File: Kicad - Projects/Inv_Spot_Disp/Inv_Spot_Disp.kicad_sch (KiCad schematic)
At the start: 44 parts, among them J1 PWM_Out, J2 Power_Supply, J3 Current_Sense, J4 Prog, SW1 1, SW2 2, SW3 3, SW4 4, SW5 SW_Push, U1 STM32F030F4Px, U2 NHD-0420H1Z, U3 AMS1117-3.3, U4 LKS561, U5 LM358, U6 LTV-817S

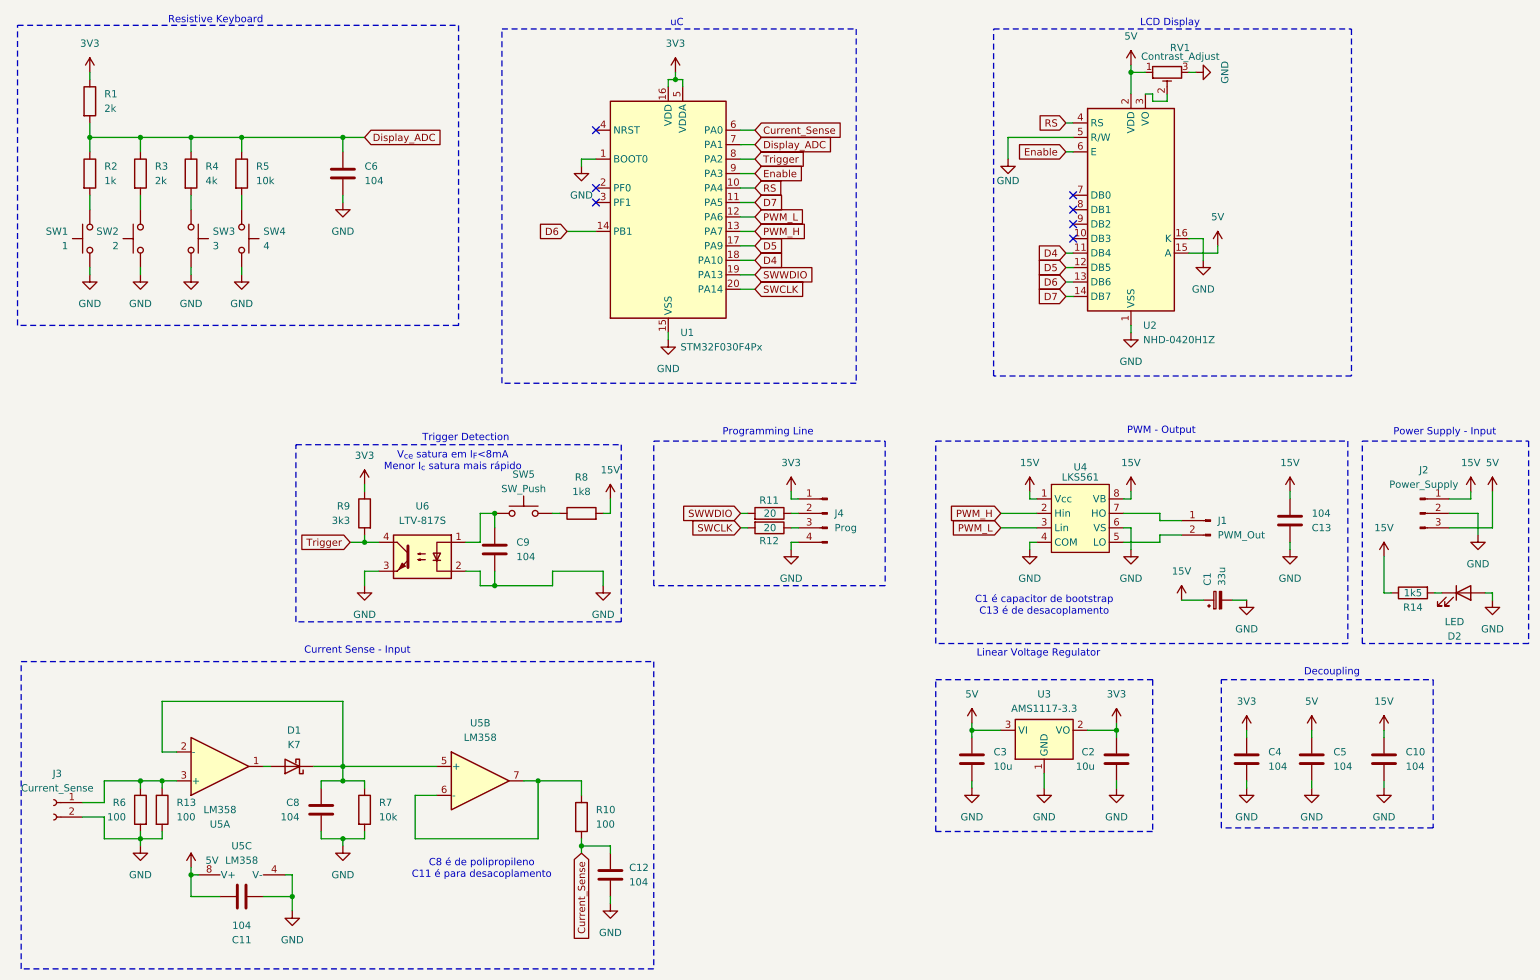
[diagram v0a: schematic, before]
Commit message: Semi-final Touches
Menu now uses power instead of current

Removed pulsed timing from "CARVAO" and "ARRUELA" operation modes

Added parafix mode

Fixed schematic for output transformer

Added rectification on the output

Trying different power trace geometry in antecipation of voltage spikes
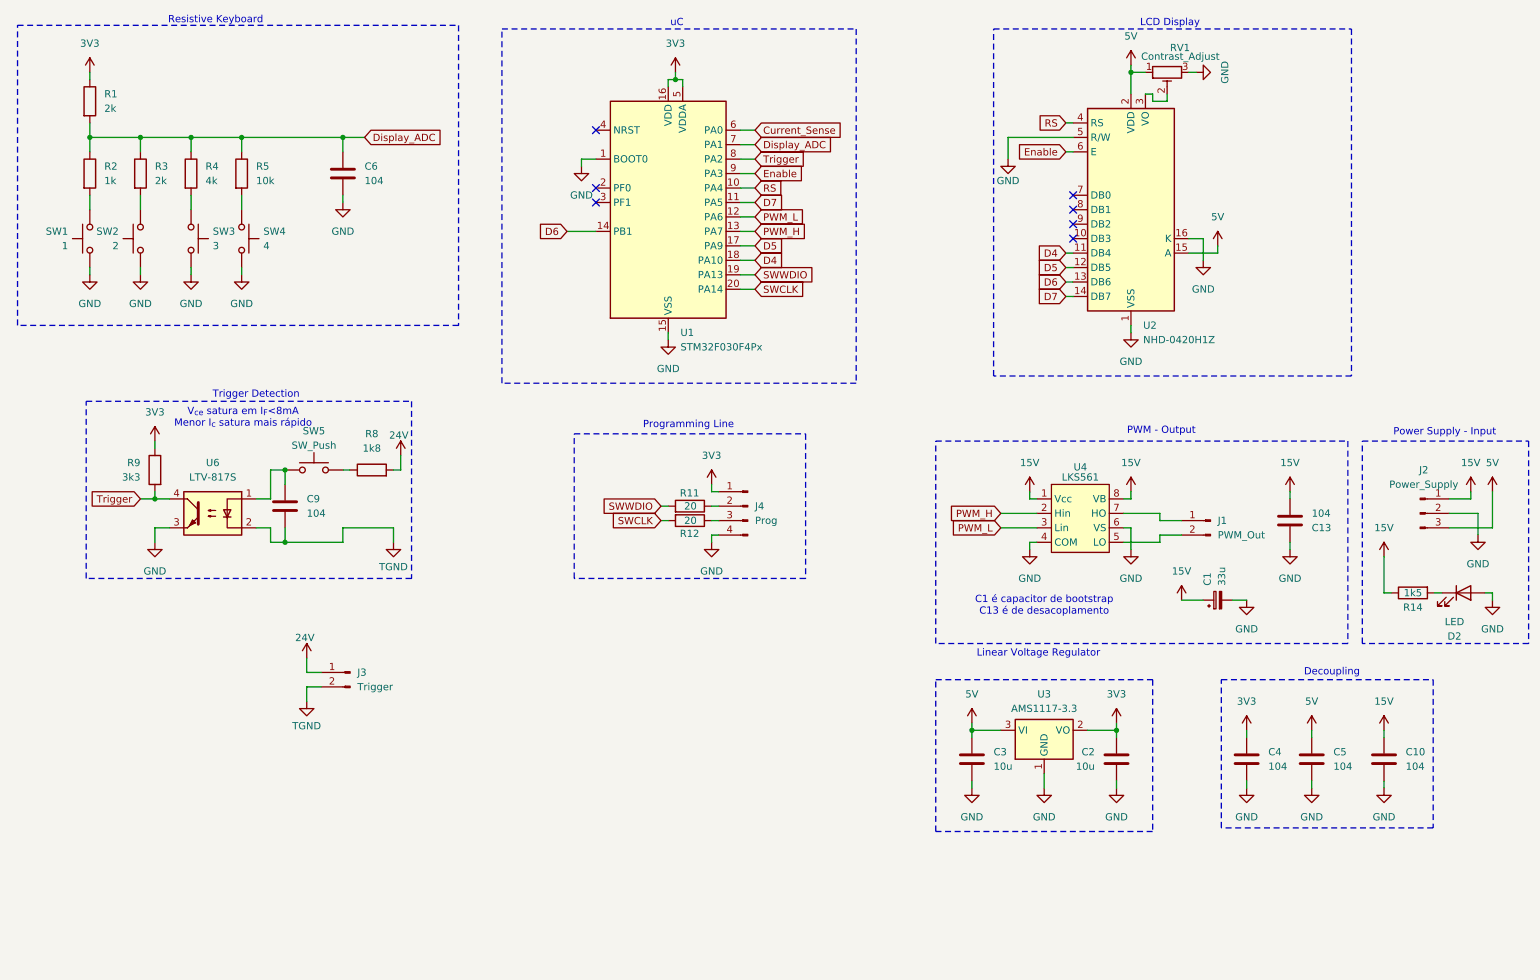
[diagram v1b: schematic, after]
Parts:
- removed C11, C12: 104, Capacitor_SMD:C_1206_3216Metric_Pad1.33x1.80mm_HandSolder, symbol Device:C
- removed C8: 104, Capacitor_THT:C_Rect_L10.0mm_W3.0mm_P7.50mm_MKS4, symbol Device:C
- removed D1: K7, Diode_SMD:D_SOD-323_HandSoldering, symbol Device:D_Schottky
- removed J3: Current_Sense, Connector_PinHeader_2.00mm:PinHeader_1x02_P2.00mm_Vertical, symbol Connector:Conn_01x02_Socket
- removed R10, R13, R6: 100, Resistor_SMD:R_1206_3216Metric_Pad1.30x1.75mm_HandSolder, symbol Device:R
- removed R7: 10k, Resistor_SMD:R_1206_3216Metric_Pad1.30x1.75mm_HandSolder, symbol Device:R
- removed U5: LM358, Package_SO:SOIC-8_3.9x4.9mm_P1.27mm, symbol Amplifier_Operational:LM358
- added J3: Trigger, Connector_PinHeader_2.54mm:PinHeader_1x02_P2.54mm_Vertical, symbol Connector:Conn_01x02_Pin
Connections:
- net 15V: no longer R8.2
- net GND: no longer C9.2, U6.2
- new net 24V: J3.1 (Pin_1), R8.2
- new net TGND: C9.2, J3.2 (Pin_2), U6.2
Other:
- note removed: "C8 é de polipropileno C11 é para desacoplamento"
- note removed: "Current Sense - Input"
- moved on the sheet: C9, J4, R11, R12, R8, R9, SW5, U6

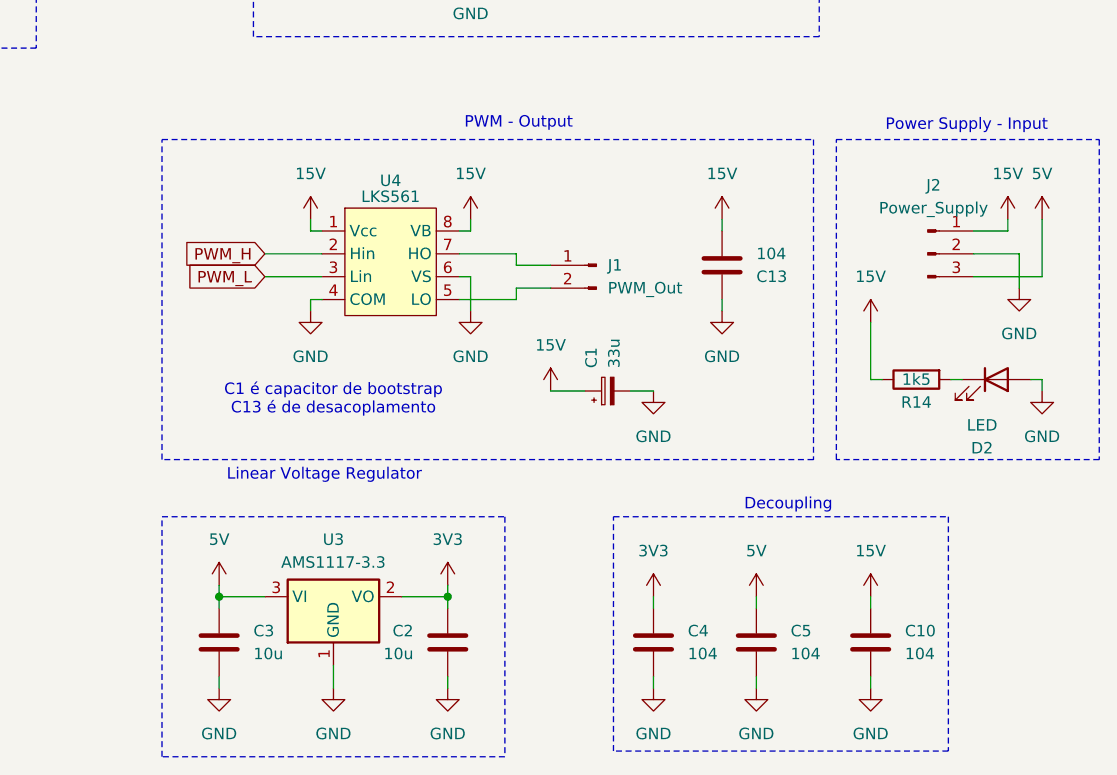
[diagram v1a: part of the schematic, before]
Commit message: Adicionado Regulador 5V - Display
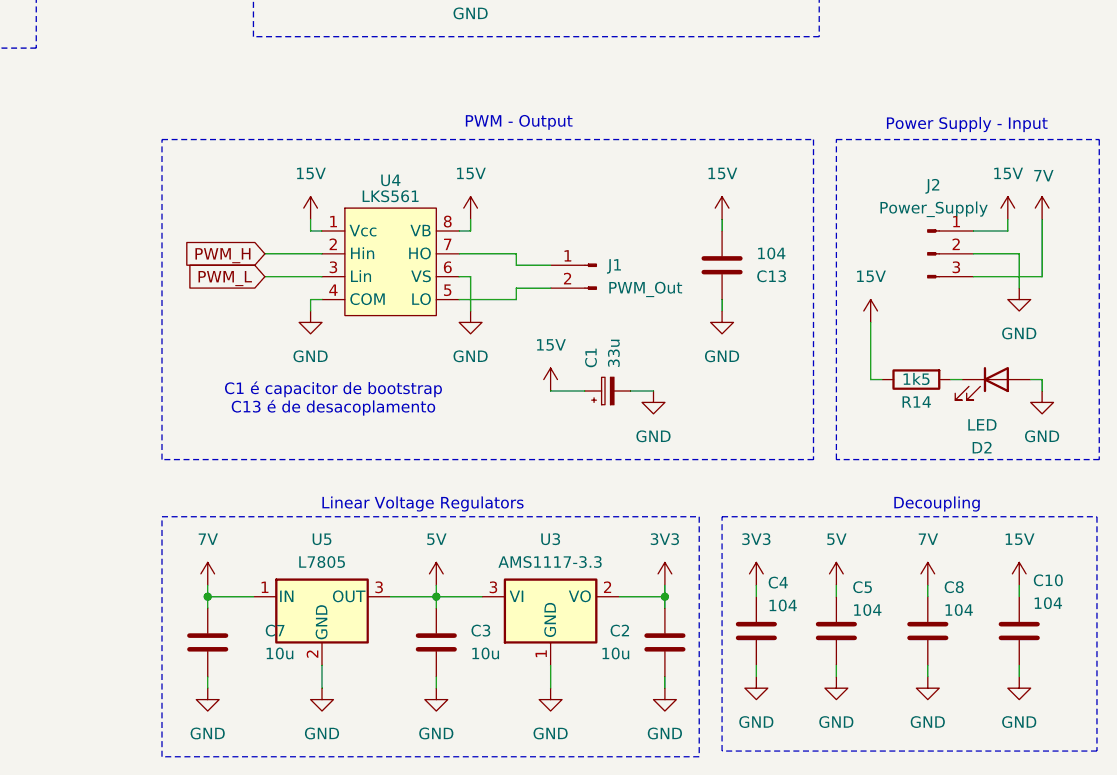
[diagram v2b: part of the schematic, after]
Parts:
- added C7: 10u, Capacitor_THT:C_Radial_D10.0mm_H12.5mm_P5.00mm, symbol Device:C
- added C8: 104, Capacitor_SMD:C_1206_3216Metric_Pad1.33x1.80mm_HandSolder, symbol Device:C
- added U5: L7805, Package_TO_SOT_SMD:TO-252-2, symbol Regulator_Linear:L7805
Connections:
- net 5V: now also U5.3 (OUT); no longer J2.3 (Pin_3)
- net GND: now also C7.2, C8.2, U5.2 (GND)
- new net 7V: C7.1, C8.1, J2.3 (Pin_3), U5.1 (IN)
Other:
- note added: "Linear Voltage Regulators"
- note removed: "Linear Voltage Regulator"
- moved on the sheet: C10, C2, C3, C4, C5, U3

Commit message: Cotações
Cotações
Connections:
- net Current_Sense: no longer names the net of U1.6 (PA0)
- no-connect marks 7 -> 8
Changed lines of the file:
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@@
+	)
+	(no_connect
+		(at 143.51 38.1)
 	)
 	(no_connect
@@
 		(pts
 			(xy 130.81 30.48) (xy 130.81 29.21)
-		)
-		(stroke
-			(width 0)
-			(type default)
-		)
-	)
-	(wire
-		(pts
-			(xy 143.51 38.1) (xy 146.05 38.1)
 		)
 		(stroke
@@
 		(property "Intersheetrefs" "${INTERSHEET_REFS}"
 			(at 151.5147 50.8 0)
-			(hide yes)
-			(show_name no)
-			(do_not_autoplace no)
-			(effects
-				(font
-					(size 1.27 1.27)
-				)
-				(justify left)
-			)
-		)
-	)
-	(global_label "Current_Sense"
-		(shape input)
-		(at 146.05 38.1 0)
-		(fields_autoplaced yes)
-		(effects
-			(font
-				(size 1.27 1.27)
-			)
-			(justify left)
-		)
-		(property "Intersheetrefs" "${INTERSHEET_REFS}"
-			(at 162.5213 38.1 0)
 			(hide yes)
 			(show_name no)
@@
 		(dnp no)
 		(property "Reference" "C7"
-			(at 189.23 147.3199 0)
+			(at 186.182 147.32 0)
 			(show_name no)
 			(do_not_autoplace no)
@@
 		)
 		(property "Value" "10u"
-			(at 189.23 149.8599 0)
-			(show_name no)
-			(do_not_autoplace no)
+			(at 186.182 149.86 0)
+			(show_name no)
+			(do_not_autoplace no)
